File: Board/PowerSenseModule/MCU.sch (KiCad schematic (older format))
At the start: 39 parts, among them J3 Programming Header, J4 Conn_01x02_Male, U2 NCV2007x, U3 dsPIC33EV32GM102, U4 MCP2542FDxMF, Y1 25 MHz

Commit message: Generated gerber and fab files
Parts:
- added J2: ISENSE, Connector_PinHeader_2.54mm:PinHeader_1x01_P2.54mm_Vertical, symbol Connector:Conn_01x01_Male
- added J5: VSENSE, Connector_PinHeader_2.54mm:PinHeader_1x01_P2.54mm_Vertical, symbol Connector:Conn_01x01_Male
- J4: value Conn_01x02_Male -> Board Interconnect
- JP1: value Jumper_NO_Small -> Program Enable
- R6: footprint Capacitor_SMD:C_0603_1608Metric_Pad1.05x0.95mm_HandSolder -> Resistor_SMD:R_0603_1608Metric_Pad1.05x0.95mm_HandSolder
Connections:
- net at R13.1, R14.2, U2.8: now also J2.1 (Pin_1)
- net at R22.2, U2.13 (-), U2.14: now also J5.1 (Pin_1)
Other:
- moved on the sheet: C9, R13
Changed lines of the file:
@@
 Sheet 2 2
 Title "Power Sense Module "
-Date ""
+Date "2019-12-18"
 Rev "1.0"
 Comp "University of Central Florida - HKN Zeta Chi"
@@
 	8100 2600 8575 2600
 Connection ~ 8100 2600
-Connection ~ 10575 1950
-Wire Wire Line
-	10725 1950 10575 1950
 Wire Wire Line
 	7025 1750 7875 1750
 Wire Wire Line
-	10575 2550 10575 2425
+	10625 2550 10625 2425
 $Comp
 L power:GNDA #PWR023
 U 1 1 5D501AF9
-P 10575 2550
-F 0 "#PWR023" H 10575 2300 50  0001 C CNN
-F 1 "GNDA" H 10580 2377 50  0000 C CNN
-F 2 "" H 10575 2550 50  0001 C CNN
-F 3 "" H 10575 2550 50  0001 C CNN
-	1    10575 2550
-	1    0    0    -1
-$EndComp
-Wire Wire Line
-	10475 1950 10575 1950
-Wire Wire Line
-	10575 2125 10575 1950
-Connection ~ 10025 1950
-Wire Wire Line
-	10175 1950 10025 1950
+P 10625 2550
+F 0 "#PWR023" H 10625 2300 50  0001 C CNN
+F 1 "GNDA" H 10630 2377 50  0000 C CNN
+F 2 "" H 10625 2550 50  0001 C CNN
+F 3 "" H 10625 2550 50  0001 C CNN
+	1    10625 2550
+	1    0    0    -1
+$EndComp
 $Comp
 L Device:C C9
 U 1 1 5D4EE1B9
-P 10575 2275
-F 0 "C9" H 10690 2321 50  0000 L CNN
-F 1 "33nF" H 10690 2230 50  0000 L CNN
-F 2 "Capacitor_SMD:C_0603_1608Metric_Pad1.05x0.95mm_HandSolder" H 10613 2125 50  0001 C CNN
-F 3 "~" H 10575 2275 50  0001 C CNN
-	1    10575 2275
+P 10625 2275
+F 0 "C9" H 10740 2321 50  0000 L CNN
+F 1 "33nF" H 10740 2230 50  0000 L CNN
+F 2 "Capacitor_SMD:C_0603_1608Metric_Pad1.05x0.95mm_HandSolder" H 10663 2125 50  0001 C CNN
+F 3 "~" H 10625 2275 50  0001 C CNN
+	1    10625 2275
 	1    0    0    -1
 $EndComp
@@
 $EndComp
 Wire Wire Line
-	10025 1950 9925 1950
-Wire Wire Line
-	10025 1400 10025 1950
-Wire Wire Line
-	9775 1400 10025 1400
-Wire Wire Line
 	9225 2050 9125 2050
 Connection ~ 9225 2050
@@
 	9225 1400 9225 1850
 Wire Wire Line
-	9475 1400 9225 1400
+	9495 1400 9225 1400
 Connection ~ 8575 2350
 Wire Wire Line
@@
 L Device:R_US R13
 U 1 1 5D4CADE5
-P 9625 1400
-F 0 "R13" V 9420 1400 50  0000 C CNN
-F 1 "75k" V 9511 1400 50  0000 C CNN
-F 2 "Resistor_SMD:R_0603_1608Metric_Pad1.05x0.95mm_HandSolder" V 9665 1390 50  0001 C CNN
-F 3 "~" H 9625 1400 50  0001 C CNN
-	1    9625 1400
+P 9645 1400
+F 0 "R13" V 9440 1400 50  0000 C CNN
+F 1 "75k" V 9531 1400 50  0000 C CNN
+F 2 "Resistor_SMD:R_0603_1608Metric_Pad1.05x0.95mm_HandSolder" V 9685 1390 50  0001 C CNN
+F 3 "~" H 9645 1400 50  0001 C CNN
+	1    9645 1400
 	0    1    1    0
 $EndComp
@@
 P 6175 1950
 F 0 "J4" H 6283 2131 50  0000 C CNN
-F 1 "Conn_01x02_Male" H 6283 2040 50  0000 C CNN
+F 1 "Board Interconnect" H 6283 2040 50  0000 C CNN
 F 2 "Connector_PinHeader_2.54mm:PinHeader_1x02_P2.54mm_Vertical" H 6175 1950 50  0001 C CNN
 F 3 "~" H 6175 1950 50  0001 C CNN
@@
 F 0 "R6" H 7093 1596 50  0000 L CNN
 F 1 "0" H 7093 1505 50  0000 L CNN
-F 2 "Capacitor_SMD:C_0603_1608Metric_Pad1.05x0.95mm_HandSolder" H 7025 1550 50  0001 C CNN
+F 2 "Resistor_SMD:R_0603_1608Metric_Pad1.05x0.95mm_HandSolder" H 7025 1550 50  0001 C CNN
 F 3 "~" H 7025 1550 50  0001 C CNN
 	1    7025 1550
@@
 P 1425 2100
 F 0 "JP1" V 1375 1900 50  0000 L CNN
-F 1 "Jumper_NO_Small" V 1425 2125 50  0000 L CNN
+F 1 "Program Enable" V 1425 2125 50  0000 L CNN
 F 2 "Connector_PinHeader_2.54mm:PinHeader_1x02_P2.54mm_Vertical" H 1425 2100 50  0001 C CNN
 F 3 "~" H 1425 2100 50  0001 C CNN
@@
 Wire Wire Line
 	7775 2450 7875 2450
+$Comp
+L Connector:Conn_01x01_Male J2
+U 1 1 5DF9BAF2
+P 10780 1570
+F 0 "J2" H 10752 1502 50  0000 R CNN
+F 1 "ISENSE" H 10765 1650 50  0000 R CNN
+F 2 "Connector_PinHeader_2.54mm:PinHeader_1x01_P2.54mm_Vertical" H 10780 1570 50  0001 C CNN
+F 3 "~" H 10780 1570 50  0001 C CNN
+	1    10780 1570
+	-1   0    0    1
+$EndComp
+Wire Wire Line
+	10475 1950 10625 1950
+Wire Wire Line
+	9925 1950 10050 1950
+Wire Wire Line
+	10050 1400 10050 1570
+Connection ~ 10050 1950
+Wire Wire Line
+	10050 1950 10175 1950
+Wire Wire Line
+	9795 1400 10050 1400
+Wire Wire Line
+	10580 1570 10050 1570
+Connection ~ 10050 1570
+Wire Wire Line
+	10050 1570 10050 1950
+Wire Wire Line
+	10600 3100 10075 3100
+Wire Wire Line
+	10075 3100 10075 3125
+Connection ~ 10075 3125
+$Comp
+L Connector:Conn_01x01_Male J5
+U 1 1 5DFA7BAD
+P 10800 3100
+F 0 "J5" H 10772 3032 50  0000 R CNN
+F 1 "VSENSE" H 10772 3123 50  0000 R CNN
+F 2 "Connector_PinHeader_2.54mm:PinHeader_1x01_P2.54mm_Vertical" H 10800 3100 50  0001 C CNN
+F 3 "~" H 10800 3100 50  0001 C CNN
+	1    10800 3100
+	-1   0    0    1
+$EndComp
+$Comp
+L F1_Logo:LOGO #G1
+U 1 1 5E098C04
+P 10870 6835
+F 0 "#G1" H 10870 6574 60  0001 C CNN
+F 1 "LOGO" H 10870 7096 60  0001 C CNN
+F 2 "" H 10870 6835 50  0001 C CNN
+F 3 "" H 10870 6835 50  0001 C CNN
+	1    10870 6835
+	1    0    0    -1
+$EndComp
+Wire Wire Line
+	10625 2125 10625 1950
+Connection ~ 10625 1950
+Wire Wire Line
+	10625 1950 10725 1950
 $EndSCHEMATC

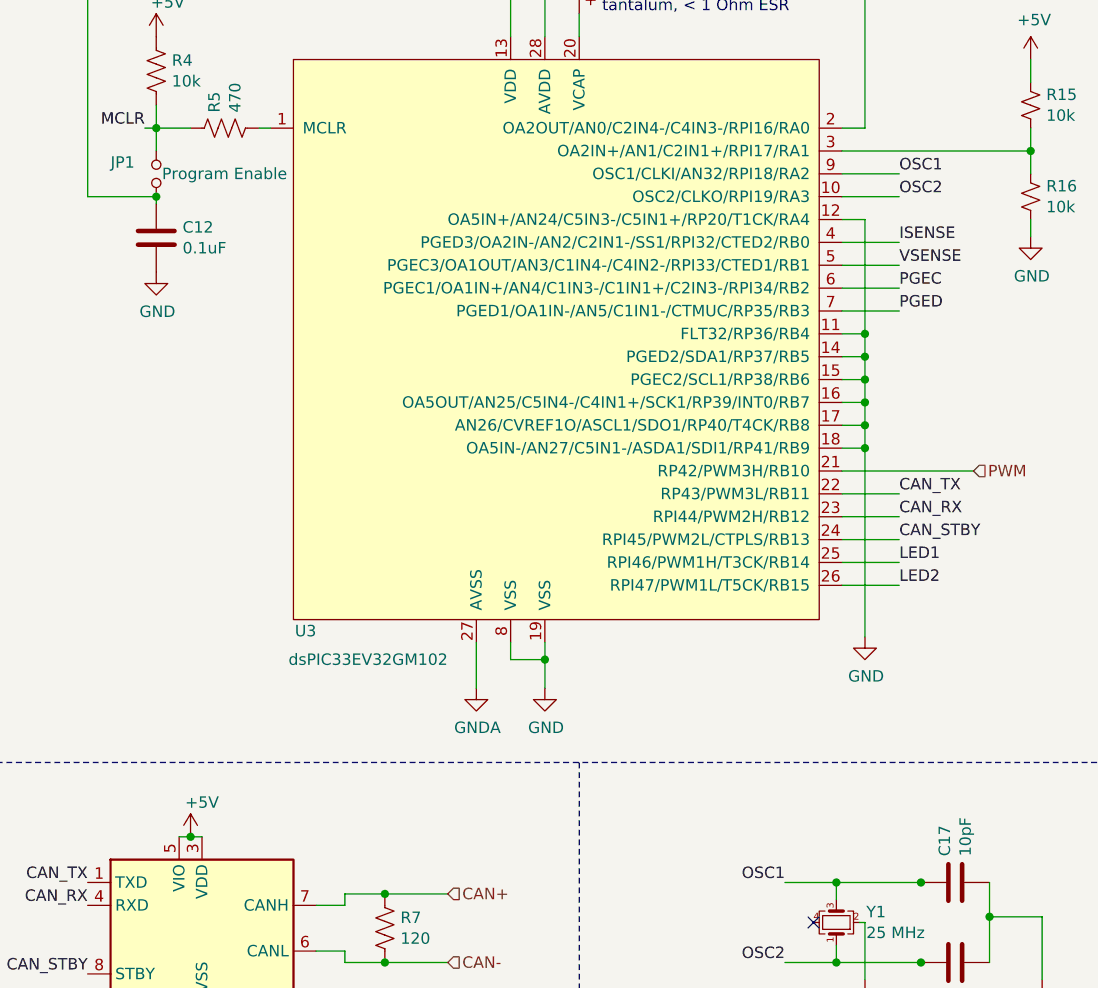
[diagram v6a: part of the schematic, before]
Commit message: Created BOM
BOM was created by adding symbol fields then using the KiCAD BOM Wizard plugin 
https://hackaday.io/project/20765-kicad-bom-wizard
Then the CSV data was imported into Excel and was tweaked.
Price per unit is about $35-40
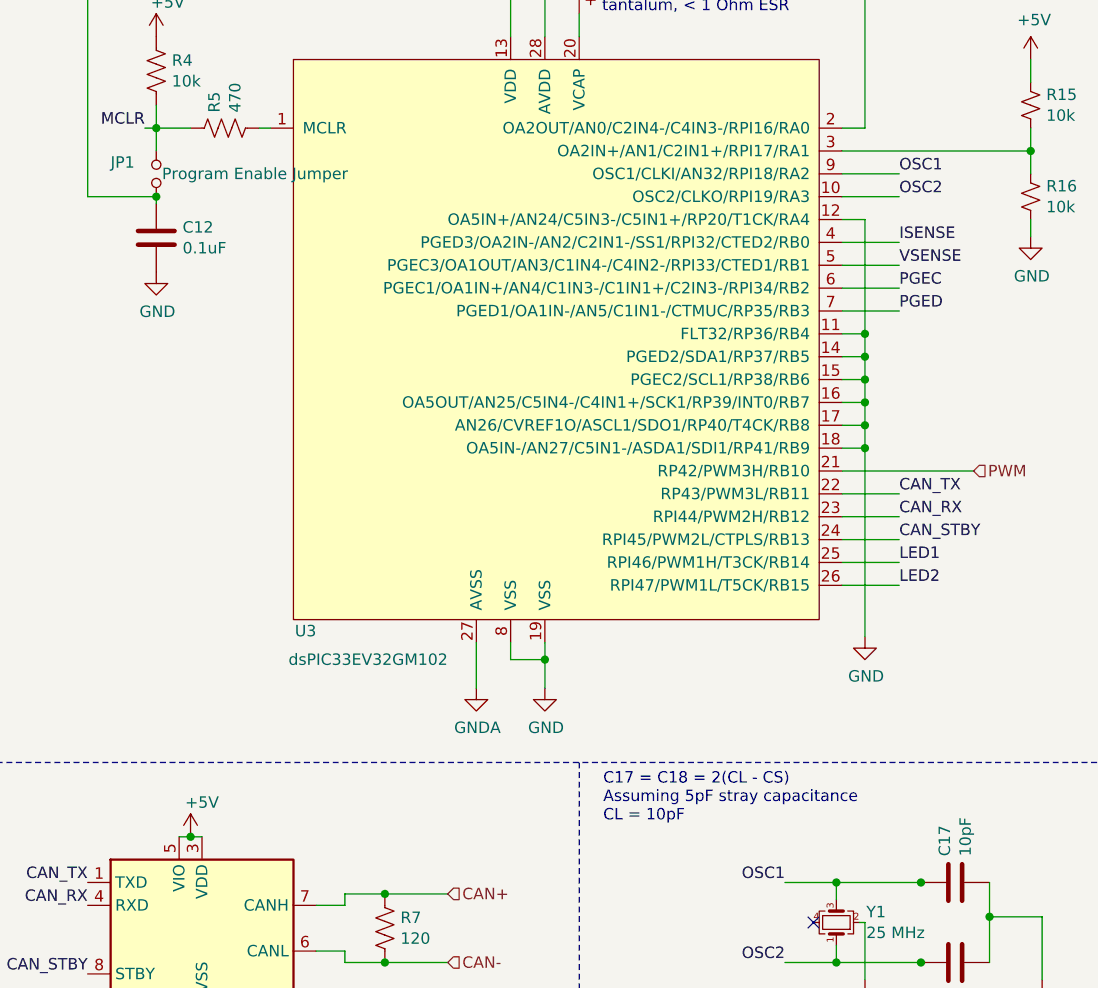
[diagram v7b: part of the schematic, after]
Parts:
- C10, C13, C24: Manufacturer (none) -> KEMET; Manufacturer PN (none) -> C0603C103J5RACTU; Price 1 QTY (none) -> 0.10; Supplier (none) -> Mouser; Supplier Link (none) -> https://www.mouser.com/ProductDetail/KEMET/C0603C103J5RACTU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; Supplier PN (none) -> 80-C0603C103J5R
- C11, C12, C14: Manufacturer (none) -> TDK; Manufacturer PN (none) -> CGA3E2X7R1H104K080AA; Price 1 QTY (none) -> 0.1; Supplier (none) -> Mouser; Supplier Link (none) -> https://www.mouser.com/ProductDetail/TDK/CGA3E2X7R1H104K080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; Supplier PN (none) -> 810-CGA3E2X7R1H104K
- C15: Manufacturer (none) -> KEMET; Manufacturer PN (none) -> T491B106K016ATAUTO; Price 1 QTY (none) -> 0.57; Supplier (none) -> Mouser; Supplier Link (none) -> https://www.mouser.com/ProductDetail/KEMET/T491B106K016ATAU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; Supplier PN (none) -> 80-T491B106K016AUTO
- C16, C9: Manufacturer (none) -> TDK; Manufacturer PN (none) -> CGA3E2X7R1H333M080AA; Price 1 QTY (none) -> 0.1; Supplier (none) -> Mouser; Supplier Link (none) -> https://www.mouser.com/ProductDetail/TDK/CGA3E2X7R1H333M080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; Supplier PN (none) -> 810-CGA3E2X7R1H333MA
- C17, C18: Manufacturer (none) -> KEMET; Manufacturer PN (none) -> C0603C100J5GAC3190; Price 1 QTY (none) -> 0.1; Supplier (none) -> Mouser; Supplier Link (none) -> https://www.mouser.com/ProductDetail/KEMET/C0603C100J5GAC31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; Supplier PN (none) -> 80-C0603C100J5G3190
- J2, J3, J4, J5: Supplier Link (none) -> https://www.amazon.com/gp/product/B07VNXL5BD/ref=ppx_yo_dt_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
- JP1: value Program Enable -> Program Enable Jumper; Supplier Link (none) -> https://www.amazon.com/gp/product/B07VNXL5BD/ref=ppx_yo_dt_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
- R10, R11: Manufacturer (none) -> Panasonic; Manufacturer PN (none) -> ERJ-PA3J122V; Price 1 QTY (none) -> 0.1; Supplier (none) -> DigiKey; Supplier Link (none) -> https://www.digikey.com/product-detail/en/panasonic-electro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; Supplier PN (none) -> P1.2KBZCT-ND
- R12, R13: Manufacturer (none) -> Panasonic; Manufacturer PN (none) -> ERJ-PA3J753V; Price 1 QTY (none) -> 0.1; Supplier (none) -> DigiKey; Supplier Link (none) -> https://www.digikey.com/product-detail/en/panasonic-electro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; Supplier PN (none) -> P75KBZCT-ND
- R14, R22: Manufacturer (none) -> Panasonic; Manufacturer PN (none) -> ERJ-PA3J102V; Price 1 QTY (none) -> 0.1; Supplier (none) -> DigiKey; Supplier Link (none) -> https://www.digikey.com/product-detail/en/panasonic-electro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; Supplier PN (none) -> P1KBZCT-ND
- R15, R16, R18, R4: Manufacturer (none) -> Panasonic; Manufacturer PN (none) -> ERJ-PA3J103V; Price 1 QTY (none) -> 0.1; Supplier (none) -> DigiKey; Supplier Link (none) -> https://www.digikey.com/product-detail/en/panasonic-electro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; Supplier PN (none) -> P10KBZCT-ND
- R17, R19: Manufacturer (none) -> Vishay / Dale; Manufacturer PN (none) -> RCS06034K99FKEA; Price 1 QTY (none) -> 0.14; Supplier (none) -> DigiKey; Supplier Link (none) -> https://www.digikey.com/product-detail/en/vishay-dale/RCS06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; Supplier PN (none) -> 541-2794-1-ND
- R20, R21: Manufacturer (none) -> Panasonic; Manufacturer PN (none) -> ERJ-PA3J301V; Price 1 QTY (none) -> 0.1; Supplier (none) -> DigiKey; Supplier Link (none) -> https://www.digikey.com/product-detail/en/panasonic-electro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; Supplier PN (none) -> P300BZCT-ND
- R5: Manufacturer (none) -> Panasonic; Manufacturer PN (none) -> ERJ-PA3J471V; Price 1 QTY (none) -> 0.1; Supplier (none) -> DigiKey; Supplier Link (none) -> https://www.digikey.com/product-detail/en/panasonic-electro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; Supplier PN (none) -> P470BZCT-ND
- R6, R9: Manufacturer (none) -> Keystone; Manufacturer PN (none) -> 5110; Price 1 QTY (none) -> 0.43; Supplier (none) -> DigiKey; Supplier Link (none) -> https://www.digikey.com/product-detail/en/keystone-electron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; Supplier PN (none) -> 36-5110CT-ND
- R7: Manufacturer (none) -> Panasonic; Manufacturer PN (none) -> ERJ-PA3J121V; Price 1 QTY (none) -> 0.1; Supplier (none) -> DigiKey; Supplier Link (none) -> https://www.digikey.com/product-detail/en/panasonic-electro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; Supplier PN (none) -> P120BZCT-ND
- R8: Price 1 QTY (none) -> 2.18
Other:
- note added: "C17 = C18 = 2(CL - CS)\nAssuming 5pF stray capacitance\nCL = 10pF"

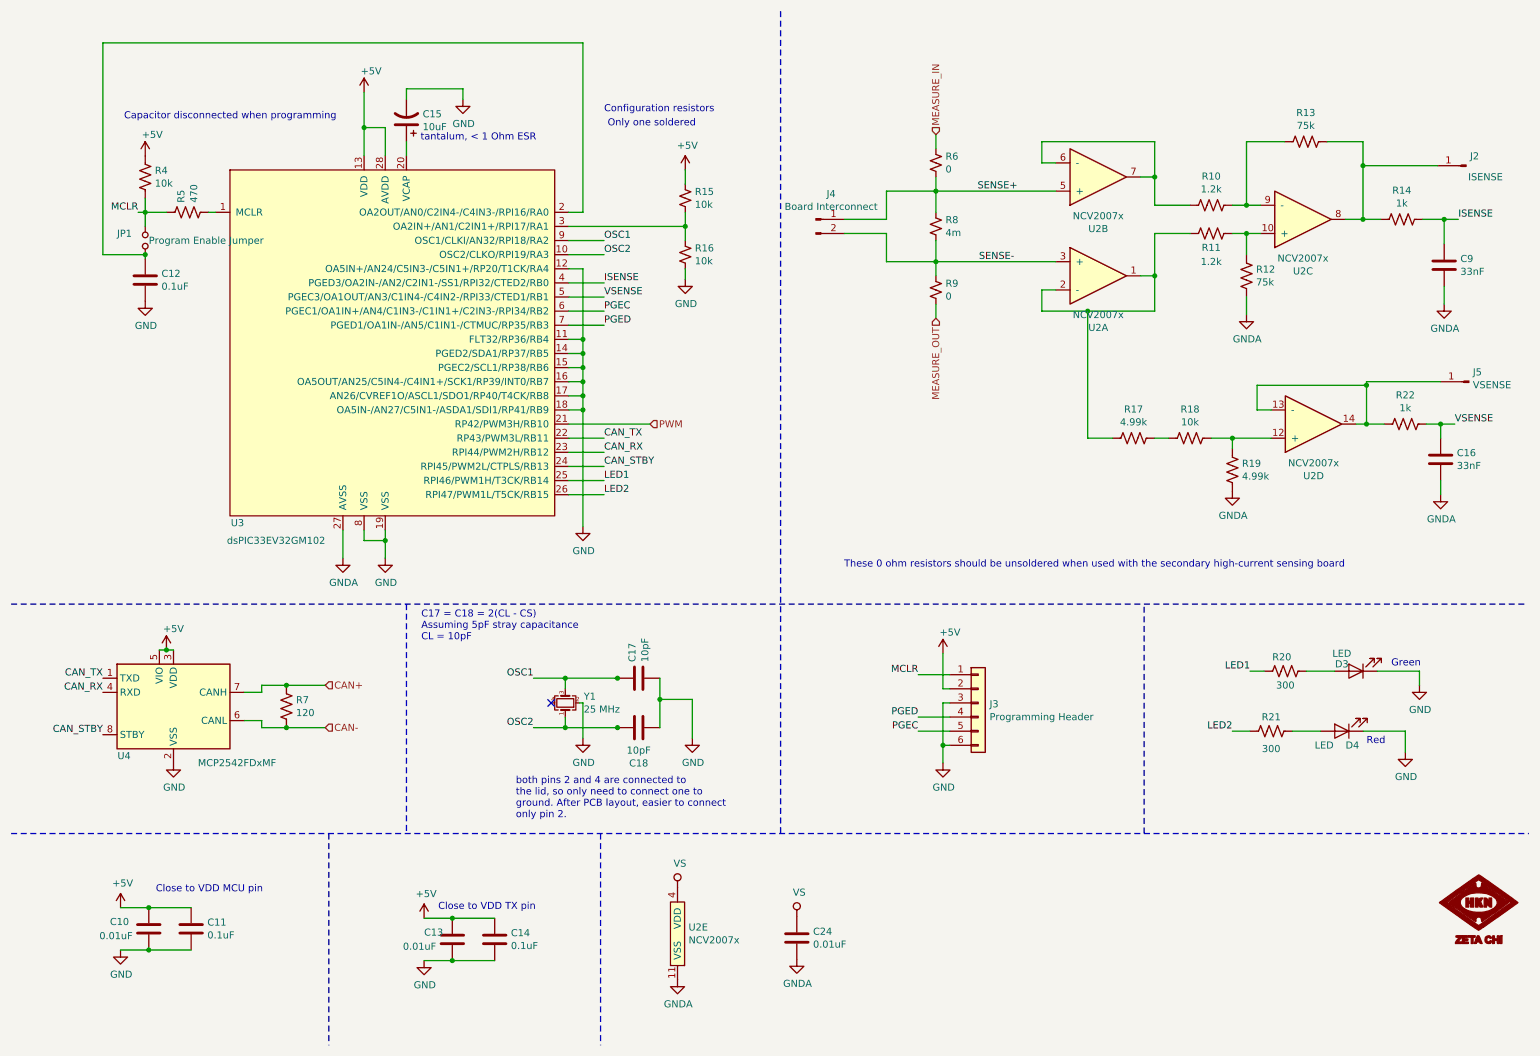
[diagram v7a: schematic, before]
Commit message: Updated BOM, schematic, PCB
- Using 3 pin jumper for program enable so that the jumper can be stored on the board
- Updated footprint for 4.7uF cap from electrolytic to smd 0805
- cleaned up some copper zones
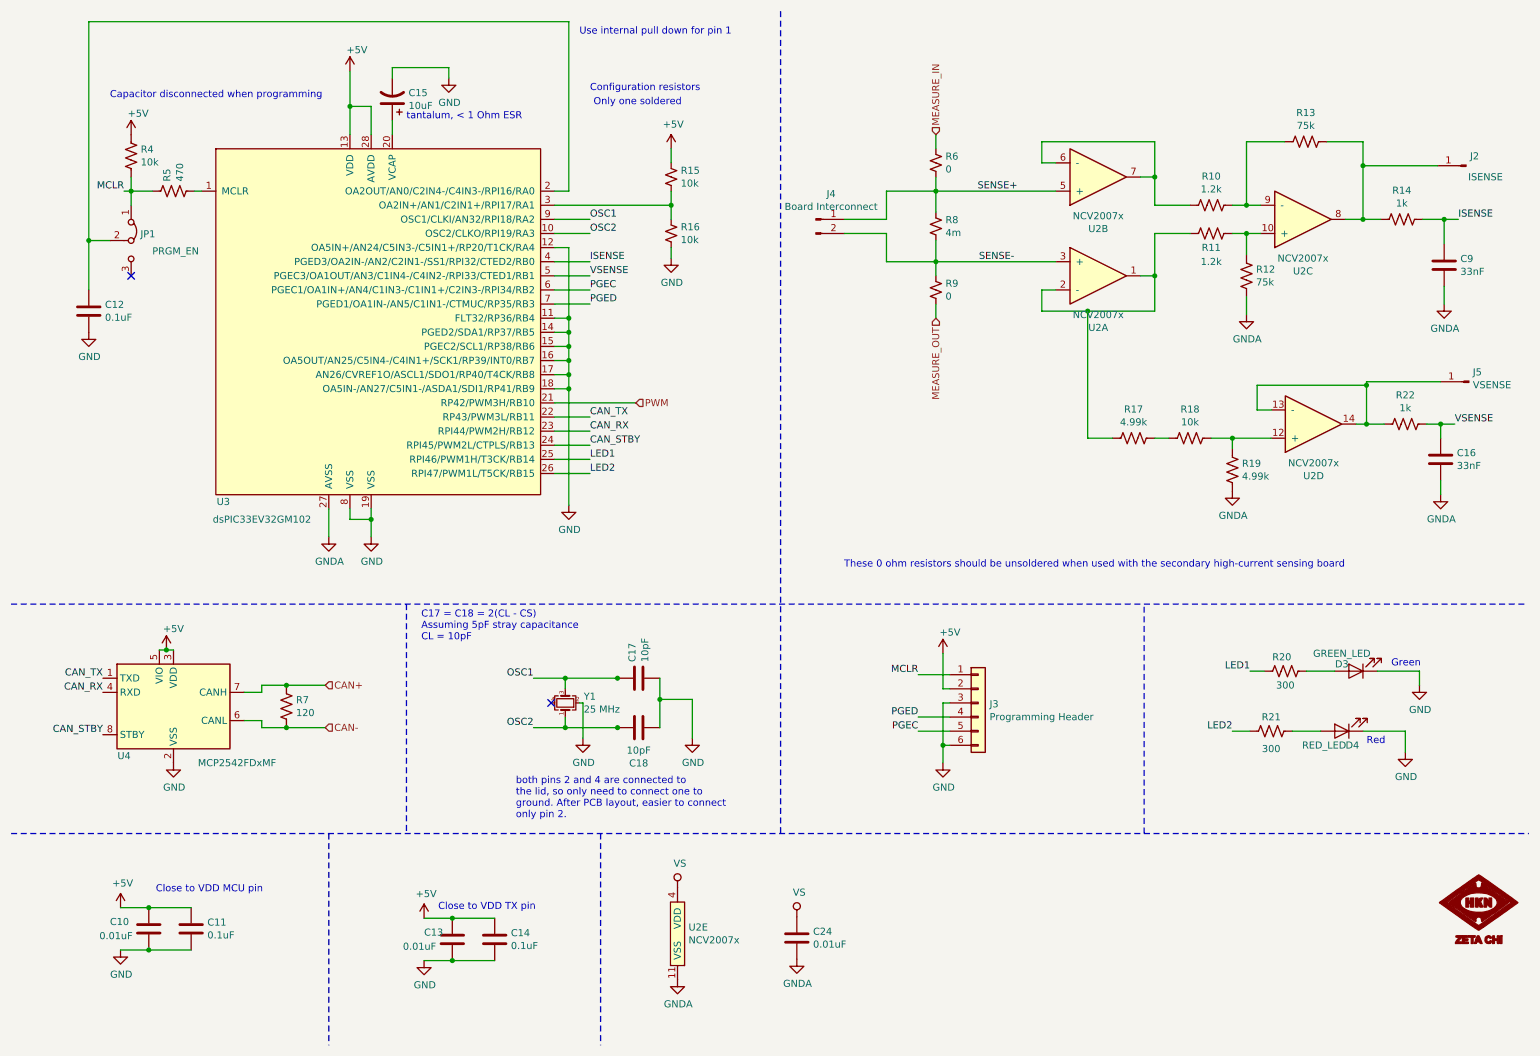
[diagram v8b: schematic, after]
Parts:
- removed JP1: Program Enable Jumper, Connector_PinHeader_2.54mm:PinHeader_1x02_P2.54mm_Vertical, symbol Device:Jumper_NO_Small
- added JP1: PRGM_EN, Connector_PinHeader_2.54mm:PinHeader_1x03_P2.54mm_Vertical, symbol Jumper:Jumper_3_Bridged12
- D3: value LED -> GREEN_LED; Manufacturer (none) -> Würth Elektronik; Manufacturer PN (none) -> 150060VS75000; Price 1 QTY (none) -> 0.14; Supplier (none) -> Digikey; Supplier Link (none) -> https://www.digikey.com/product-detail/en/w-rth-elektronik/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; Supplier PN (none) -> 732-4980-1-ND
- D4: value LED -> RED_LED; Manufacturer (none) -> Würth Elektronik; Manufacturer PN (none) -> 150060RS75000; Price 1 QTY (none) -> 0.14; Supplier (none) -> Digikey; Supplier Link (none) -> https://www.digikey.com/product-detail/en/w-rth-elektronik/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; Supplier PN (none) -> 732-4978-1-ND
- R10, R11, R12, R13, R14, R15, R16, R17, R18, R19, R20, R21, R22, R4, R5, R6, R7, R9: Supplier DigiKey -> Digikey
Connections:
- net MCLR: now also JP1.1 (A)
- net at C12.1, U3.2 (OA2OUT/AN0/C2IN4-/C4IN3-/RPI16/RA0): now also JP1.2 (C)
- no-connect marks 1 -> 2
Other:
- note added: "Use internal pull down for pin 1"
- moved on the sheet: C12, C15, R15, R16, R4, R5, U3
